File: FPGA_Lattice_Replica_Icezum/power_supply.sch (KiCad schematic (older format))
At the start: 53 parts, among them J18 Power_Jack, Q1 DMP3017, Q2 DMP3017, Q3 DMP2035U-7, Q4 Mosfet_P_DFN-6, Q5 PMBT3906, SW3 SPDT_Switch, SW4 Switch, U10 AP7361, U11 TLV711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

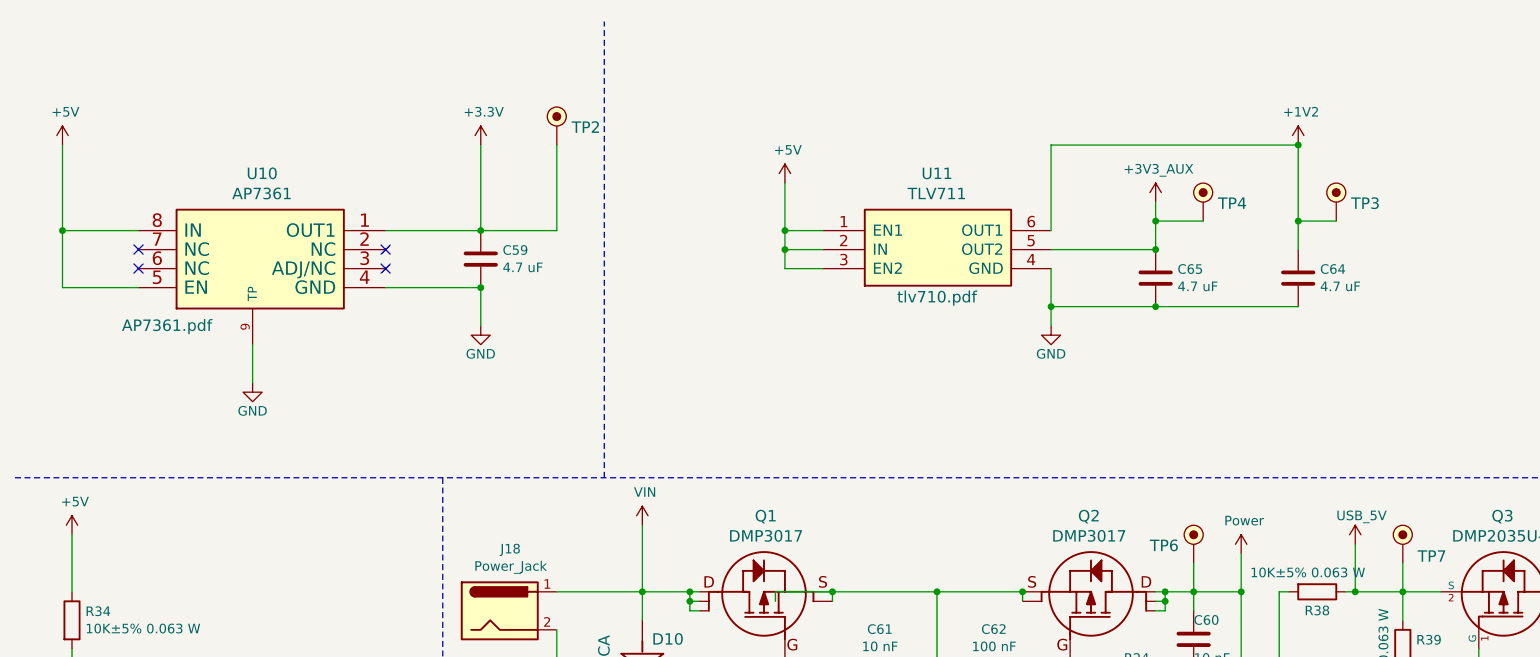
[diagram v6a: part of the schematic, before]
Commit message: se agregaron mas comentarios a las hojas estado del esquematico: finalizado
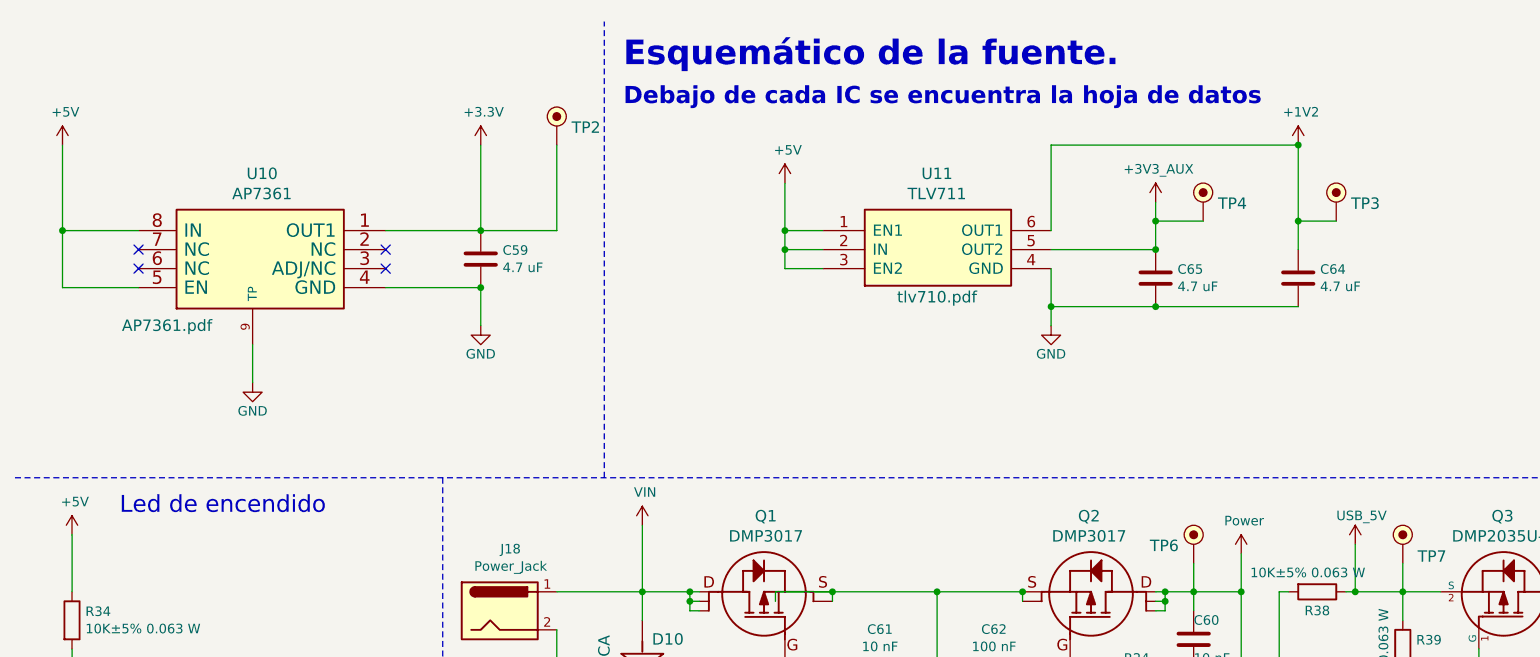
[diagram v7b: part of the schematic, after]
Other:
- note added: "Debajo de cada IC se encuentra la hoja de datos\n"
- note added: "Esquemático de la fuente. \n"
- note added: "Led de encendido"
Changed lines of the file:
@@
 Text Notes 9200 1100 0    129  ~ 26
 General \npower \nflags
+Text Notes 3700 750  0    129  ~ 26
+Esquemático de la fuente. \n
+Text Notes 3700 950  0    90   ~ 18
+Debajo de cada IC se encuentra la hoja de datos\n
+Text Notes 1050 3100 0    89   ~ 0
+Led de encendido
 $EndSCHEMATC

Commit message: se corrigieron errores de huellas y referencias que genereban errores cuando se hacia el diseño PCB
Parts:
- D12: symbol Device:LED -> icezum:LED
- D2, D4: footprint footprints:LED_0603 -> footprints:SOD-323
- Q5: symbol Transistor_BJT:PMBT3906YS -> icezum:PNP
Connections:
- net GND: now also D12.K; no longer D12.1 (K)
- net Power: now also Q5.2 (E); no longer Q5.1 (E1)
- net USB_5V: now also R38.2; no longer R38.1
- net at R28.2: now also Q5.3 (C); no longer Q5.6 (C1)
- net at R34.2: now also D12.A; no longer D12.2 (A)
- new net: Q5.1 (B), R38.1
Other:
- moved on the sheet: R38
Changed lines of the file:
@@
 $EndComp
 $Comp
-L Transistor_BJT:PMBT3906YS Q5
+L icezum:PNP Q5
 U 1 1 5CF8E236
-P 7150 4350
-F 0 "Q5" V 7385 4350 50  0000 C CNN
-F 1 "PMBT3906" V 7476 4350 50  0000 C CNN
-F 2 "footprints:SOT-23" H 7350 4450 50  0001 C CNN
-F 3 "https://assets.nexperia.com/documents/data-sheet/PMBT3906YS.pdf" H 7150 4350 50  0001 C CNN
-	1    7150 4350
+P 7250 4450
+F 0 "Q5" V 7400 4450 50  0000 C CNN
+F 1 "PMBT3906" V 7500 4450 50  0000 C CNN
+F 2 "footprints:SOT-23" H 7450 4550 50  0001 C CNN
+F 3 "https://assets.nexperia.com/documents/data-sheet/PMBT3906YS.pdf" H 7250 4450 50  0001 C CNN
+	1    7250 4450
 	0    1    1    0
 $EndComp
@@
 F 0 "D2" V 9200 4950 60  0000 R CNN
 F 1 "BZX384C5V1-E3" H 9250 5150 60  0000 R CNN
-F 2 "footprints:LED_0603" H 8750 5000 60  0001 C CNN
+F 2 "footprints:SOD-323" H 8750 5000 60  0001 C CNN
 F 3 "" H 8750 5000 60  0000 C CNN
 	1    8750 5000
@@
 L Device:R R38
 U 1 1 5CF66502
-P 7350 3500
-F 0 "R38" V 7450 3500 50  0000 C CNN
-F 1 "10K±5% 0.063 W" V 7250 3450 50  0000 C CNN
-F 2 "footprints:R_0402" V 7280 3500 50  0001 C CNN
-F 3 "~" H 7350 3500 50  0001 C CNN
-	1    7350 3500
-	0    1    1    0
+P 7250 3750
+F 0 "R38" V 7150 3750 50  0000 C CNN
+F 1 "10K±5% 0.063 W" V 7350 3800 50  0000 C CNN
+F 2 "footprints:R_0402" V 7180 3750 50  0001 C CNN
+F 3 "~" H 7250 3750 50  0001 C CNN
+	1    7250 3750
+	-1   0    0    1
 $EndComp
 $Comp
@@
 U 1 1 5CF69DD6
 P 6950 5100
-F 0 "SW3" H 7325 5441 47  0000 C CNN
-F 1 "SPDT_Switch" H 7325 5354 47  0000 C CNN
+F 0 "SW3" H 7150 5000 47  0000 C CNN
+F 1 "SPDT_Switch" H 7150 4900 47  0000 C CNN
 F 2 "footprints:slide-sw-spdt-right-angle" H 6950 5100 60  0001 C CNN
 F 3 "" H 6950 5100 60  0000 C CNN
@@
 Wire Wire Line
 	7950 4450 8200 4450
-Wire Wire Line
-	7350 4450 7650 4450
-Wire Wire Line
-	7150 4150 7150 3500
 Wire Wire Line
 	7800 3650 7800 3500
@@
 Wire Wire Line
 	6700 3500 6950 3500
-Connection ~ 6950 3500
-Wire Wire Line
-	6950 3500 6950 4450
 $Comp
 L icezum:+5V #PWR090
@@
 Wire Wire Line
 	7800 3350 7800 3500
-Wire Wire Line
-	7150 3500 7200 3500
 $Comp
 L icezum:USB_5V #PWR087
@@
 	1    0    0    -1
 $EndComp
-Wire Wire Line
-	7500 3500 7550 3500
 Wire Wire Line
 	7550 3250 7550 3500
@@
 F 0 "D4" H 9850 6450 50  0000 C CNN
 F 1 "NSR0530HT1G" H 9850 6250 50  0000 C CNN
-F 2 "footprints:LED_0603" H 9850 6350 50  0001 C CNN
+F 2 "footprints:SOD-323" H 9850 6350 50  0001 C CNN
 F 3 "" H 9850 6350 50  0000 C CNN
 	1    9850 6350
@@
 RESET
 $Comp
-L Device:LED D12
+L icezum:LED D12
 U 1 1 5CFFD73A
-P 800 4300
-F 0 "D12" V 839 4182 50  0000 R CNN
-F 1 "WHITE" V 748 4182 50  0000 R CNN
-F 2 "footprints:LED_0603" H 800 4300 50  0001 C CNN
-F 3 "~" H 800 4300 50  0001 C CNN
-	1    800  4300
-	0    -1   -1   0
+P 800 4100
+F 0 "D12" V 1200 4050 50  0000 R CNN
+F 1 "WHITE" V 950 4350 50  0000 R CNN
+F 2 "footprints:LED_0603" H 800 4100 50  0001 C CNN
+F 3 "~" H 800 4100 50  0001 C CNN
+	1    800  4100
+	0    1    1    0
 $EndComp
 $Comp
@@
 Wire Wire Line
 	800  3200 800  3500
-Wire Wire Line
-	800  3800 800  4150
 Wire Notes Line
 	500  2900 9150 2900
@@
 Wire Wire Line
 	3350 3700 3350 4550
-Wire Wire Line
-	800  4450 800  4950
 $Comp
 L power:GND #PWR0114
@@
 Text Notes 1050 3100 0    89   ~ 0
 Led de encendido
+Wire Wire Line
+	7550 4450 7650 4450
+Wire Wire Line
+	6950 3500 6950 4450
+Connection ~ 6950 3500
+Wire Wire Line
+	7250 3500 7250 3600
+Wire Wire Line
+	7250 3500 7550 3500
+Wire Wire Line
+	7250 3900 7250 4000
+Wire Wire Line
+	800  3800 800  4100
+Wire Wire Line
+	800  4650 800  4950
 $EndSCHEMATC
